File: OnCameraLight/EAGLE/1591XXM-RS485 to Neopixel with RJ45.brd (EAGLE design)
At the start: 54 x 29 mm, 8 parts, among them IC1 75176AP, J1 RJHSE-5381

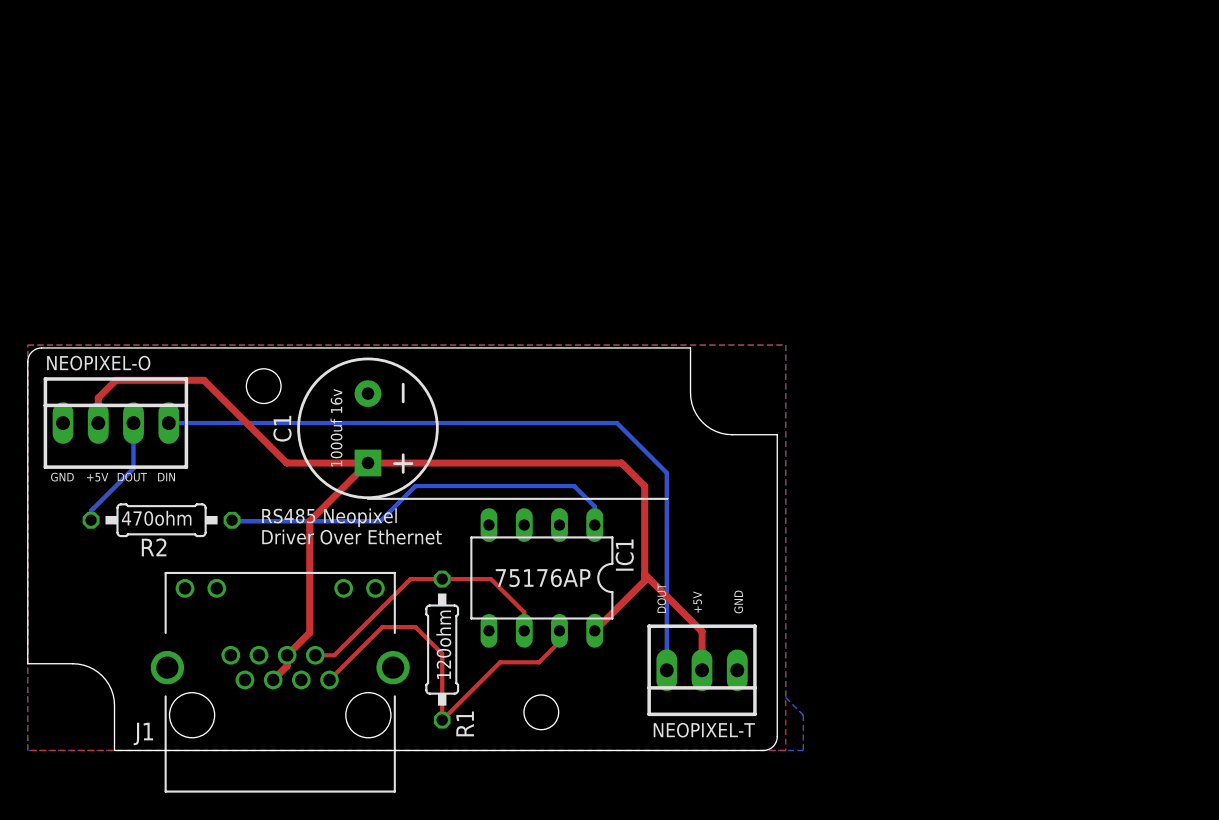
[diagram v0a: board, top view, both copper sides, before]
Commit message: Some more designs to fit different Hammond enclosures.
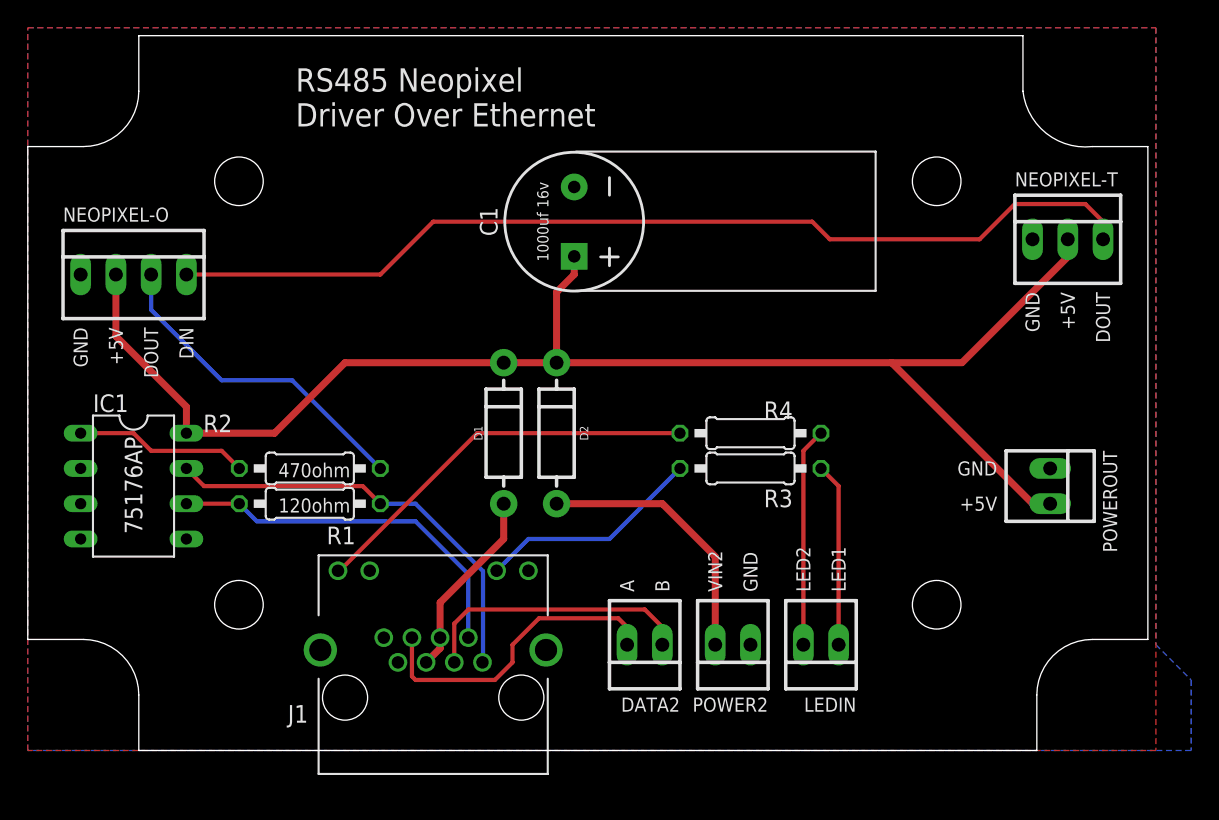
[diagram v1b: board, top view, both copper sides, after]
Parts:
- removed BOX1: HAMMOND-BOX-1551H, hammond:1551H
- added D1, D2: 1A/50V/1.1V, SparkFun-DiscreteSemi:DIODE-1N4001
- added DATA2, LEDIN, POWER2, POWEROUT: 22-23-2021, con-molex:22-23-2021
- added R3, R4: (no value), rcl:0207/10
- added U$1: (no value), hammond:1591XXM
- moved NEOPIXEL-T 40.7 mm to (74.9, 36.8), turned to 0 degrees
- moved IC1 30.2 mm to (7.62, 19.1), turned to 270 degrees
- moved C1 21.0 mm to (39.4, 38.1)
- moved R1 14.2 mm to (20.3, 17.8), turned to 0 degrees
- moved R2 11.3 mm to (20.3, 20.3), turned to 0 degrees
- moved J1 11.1 mm to (29.2, 3.81)
- moved NEOPIXEL-O 10.8 mm to (7.62, 34.3)
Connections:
- removed net DATA2+: J1.3
- removed net DATA2-: J1.6
- removed net RS485+: IC1.7, J1.1, R1.1
- removed net RS485-: IC1.6, J1.2, R1.2
- new net DATA1A: IC1.6, J1.2, R1.1
- new net DATA1B: IC1.7, J1.1, R1.2
- new net DATA2A: DATA2.2, J1.6
- new net DATA2B: DATA2.1, J1.3
- new net LED1IN: LEDIN.1, R3.1
- new net LED2IN: LEDIN.2, R4.1
- new net VIN1: D1.A, J1.4, J1.5
- new net VIN2: D2.A, POWER2.2
- net GND: now also POWER2.1, POWEROUT.1
- net LED1: now also R3.2
- net LED2: now also R4.2
- net VCC: now also D1.C, D2.C, POWEROUT.2; no longer J1.4, J1.5
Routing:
- net DATA1B: track 0.00 -> 31.0 mm
- net LED2: track 0.00 -> 28.7 mm
- net DATA1A: track 0.00 -> 27.0 mm
- net RS485+: track 26.8 -> 0.00 mm
- net VCC: track 83.9 -> 107.4 mm
- net DATA2A: track 0.00 -> 22.5 mm
- net DATA2B: track 0.00 -> 20.0 mm
- net RS485-: track 19.6 -> 0.00 mm
- net NEO-T: track 51.6 -> 71.0 mm
- net VIN2: track 0.00 -> 19.4 mm
- net NEODATA: track 29.2 -> 12.5 mm
- net LED1: track 0.00 -> 16.3 mm
- net LED2IN: track 0.00 -> 15.8 mm
- net NEO-O: track 8.27 -> 23.8 mm
- net VIN1: track 0.00 -> 13.7 mm
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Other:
- board size 54 x 29 mm -> 80.7 x 51.5 mm
- board text added: "A"
- board text added: "B"
- board text added: "Fits Hammond 1591XXM"
- board text added: "LED1"
- board text added: "LED2"
- board text added: "VIN2"
- board text removed: "Fits Hammond 1551H"

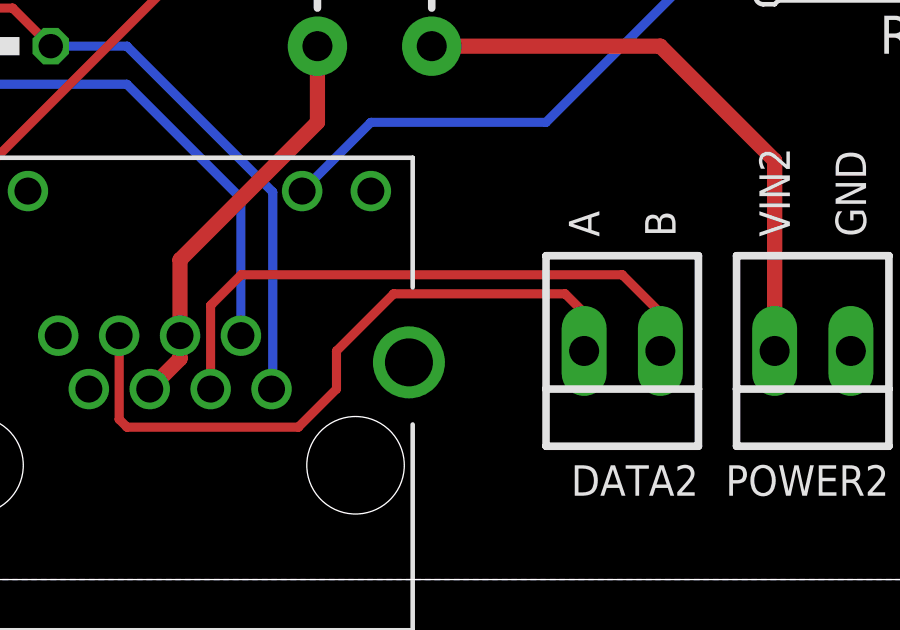
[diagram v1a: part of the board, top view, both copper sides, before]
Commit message: Go through and fix notation on RS485 wiring everywhere to use the standard A/B notation.
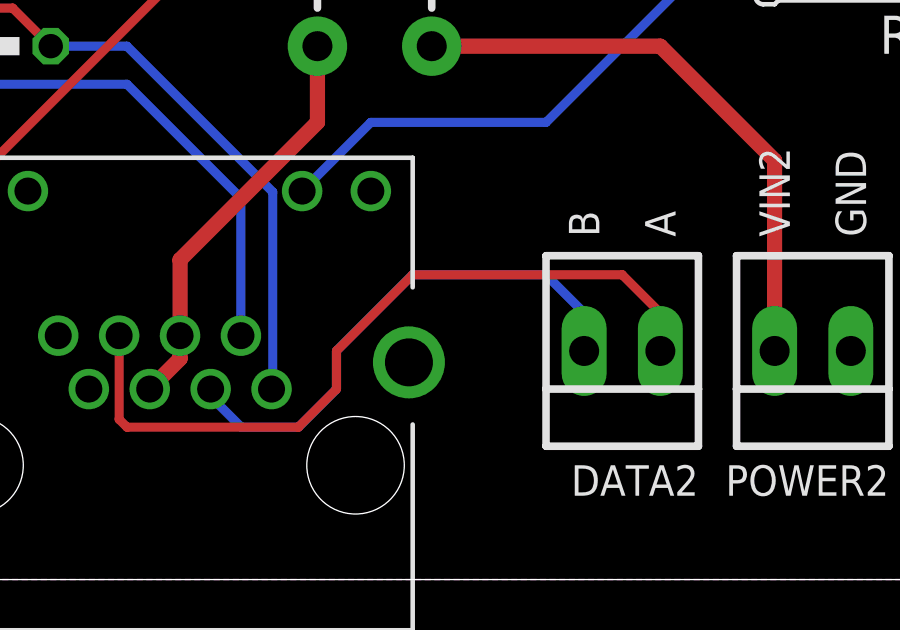
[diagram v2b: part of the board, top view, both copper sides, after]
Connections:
- net DATA2A: now also DATA2.1; no longer DATA2.2
- net DATA2B: now also DATA2.2; no longer DATA2.1
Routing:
- net DATA2A: track 22.5 -> 25.6 mm
- net DATA2B: track 20.0 -> 17.8 mm
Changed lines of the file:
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@@
 <drawing>
 <settings>
-<setting alwaysvectorfont="yes"/>
+<setting alwaysvectorfont="no"/>
 <setting verticaltext="up"/>
 </settings>
-<grid distance="50" unitdist="mil" unit="mil" style="lines" multiple="1" display="no" altdistance="5" altunitdist="mil" altunit="mil"/>
+<grid distance="25" unitdist="mil" unit="mil" style="lines" multiple="1" display="no" altdistance="5" altunitdist="mil" altunit="mil"/>
 <layers>
 <layer number="1" name="Top" color="4" fill="1" visible="yes" active="yes"/>
@@
 <text x="52.07" y="11.43" size="1.016" layer="25" rot="R90" align="center-left">GND</text>
 <text x="49.53" y="11.43" size="1.016" layer="25" rot="R90" align="center-left">VIN2</text>
-<text x="43.18" y="11.43" size="1.016" layer="25" rot="R90" align="center-left">A</text>
-<text x="45.72" y="11.43" size="1.016" layer="25" rot="R90" align="center-left">B</text>
+<text x="43.18" y="11.43" size="1.016" layer="25" rot="R90" align="center-left">B</text>
+<text x="45.72" y="11.43" size="1.016" layer="25" rot="R90" align="center-left">A</text>
 <text x="55.88" y="11.43" size="1.016" layer="25" rot="R90" align="center-left">LED2</text>
 <text x="58.42" y="11.43" size="1.016" layer="25" rot="R90" align="center-left">LED1</text>
@@
 <signal name="DATA2B">
 <contactref element="J1" pad="3"/>
-<contactref element="DATA2" pad="1"/>
-<wire x1="30.73" y1="6.35" x2="30.73" y2="9.14" width="0.3048" layer="1"/>
-<wire x1="31.75" y1="10.16" x2="44.45" y2="10.16" width="0.3048" layer="1"/>
-<wire x1="44.45" y1="10.16" x2="45.72" y2="8.89" width="0.3048" layer="1"/>
-<wire x1="45.72" y1="8.89" x2="45.72" y2="7.62" width="0.3048" layer="1"/>
-<wire x1="30.73" y1="9.14" x2="31.75" y2="10.16" width="0.3048" layer="1"/>
+<contactref element="DATA2" pad="2"/>
+<wire x1="30.73" y1="6.35" x2="30.73" y2="6.1" width="0.3048" layer="16"/>
+<wire x1="30.73" y1="6.1" x2="31.75" y2="5.08" width="0.3048" layer="16"/>
+<wire x1="31.75" y1="5.08" x2="33.655" y2="5.08" width="0.3048" layer="16"/>
+<wire x1="33.655" y1="5.08" x2="34.925" y2="6.35" width="0.3048" layer="16"/>
+<wire x1="34.925" y1="6.35" x2="34.925" y2="7.62" width="0.3048" layer="16"/>
+<wire x1="34.925" y1="7.62" x2="37.465" y2="10.16" width="0.3048" layer="16"/>
+<wire x1="41.91" y1="10.16" x2="43.18" y2="8.89" width="0.3048" layer="16"/>
+<wire x1="43.18" y1="8.89" x2="43.18" y2="7.62" width="0.3048" layer="16"/>
+<wire x1="37.465" y1="10.16" x2="41.91" y2="10.16" width="0.3048" layer="16"/>
 </signal>
 <signal name="DATA2A">
 <contactref element="J1" pad="6"/>
-<contactref element="DATA2" pad="2"/>
 <wire x1="27.68" y1="8.13" x2="27.68" y2="5.34" width="0.3048" layer="1"/>
 <wire x1="27.68" y1="5.34" x2="27.94" y2="5.08" width="0.3048" layer="1"/>
 <wire x1="27.94" y1="5.08" x2="33.655" y2="5.08" width="0.3048" layer="1"/>
 <wire x1="33.655" y1="5.08" x2="34.925" y2="6.35" width="0.3048" layer="1"/>
-<wire x1="36.83" y1="9.525" x2="42.545" y2="9.525" width="0.3048" layer="1"/>
-<wire x1="42.545" y1="9.525" x2="43.18" y2="8.89" width="0.3048" layer="1"/>
-<wire x1="43.18" y1="8.89" x2="43.18" y2="7.62" width="0.3048" layer="1"/>
-<wire x1="34.925" y1="6.35" x2="34.925" y2="7.62" width="0.3048" layer="1"/>
-<wire x1="34.925" y1="7.62" x2="36.83" y2="9.525" width="0.3048" layer="1"/>
+<wire x1="34.925" y1="7.62" x2="34.925" y2="6.35" width="0.3048" layer="1"/>
+<contactref element="DATA2" pad="1"/>
+<wire x1="45.72" y1="7.62" x2="45.72" y2="8.89" width="0.3048" layer="1"/>
+<wire x1="45.72" y1="8.89" x2="44.45" y2="10.16" width="0.3048" layer="1"/>
+<wire x1="44.45" y1="10.16" x2="37.465" y2="10.16" width="0.3048" layer="1"/>
+<wire x1="37.465" y1="10.16" x2="34.925" y2="7.62" width="0.3048" layer="1"/>
 </signal>
 </signals>
